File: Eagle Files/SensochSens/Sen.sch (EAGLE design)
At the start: 15 parts, among them U2 MIC5219, X1 ADC0-7

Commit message: 
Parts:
- removed C5: 1uF, SparkFun-Passives:CAP0402-CAP
- removed I2C_BUS: I2C_BUS, SparkFun-Connectors:M021X02_NO_SILK
- removed LED2: RED, SparkFun-LED:LED0603
- removed R6: 1k, SparkFun-Passives:RESISTOR0402-RES
- removed RN1: (no value), resistor-net:RN08
- removed X1: ADC0-7, con-molex:53047-10
- added C2: 10uF, SparkFun-Passives:CAP_POL1206
- added JP3: I2C_BUS, SparkFun-Connectors:M021X02_NO_SILK
- added LED1: RED, SparkFun-LED:LED0603
- added R1: 100k, SparkFun-Passives:RESISTOR0402-RES
- added RN2: (no value), resistor-net:RN08
- added X2: ADC0-7, con-molex:53047-10
- C4: value 10uF -> 1uF; device SparkFun-Passives:CAP_POL1206 -> SparkFun-Passives:CAP0402-CAP
- JP1: value LIPO_charger -> FTDI_BASICPTH; device jumper:JP4E -> SparkFun-Connectors:FTDI_BASICPTH
- JP2: value FTDI_BASICPTH -> LIPO_charger; device SparkFun-Connectors:FTDI_BASICPTH -> jumper:JP4E
- R2: value 100k -> 1k
- renumbered SMD1 to U1
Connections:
- removed net N$7: LED2.A, R6.1
- new net N$2: LED1.A, R2.1
- net 3.3V: now also C3.+, C4.1, JP1.4, R1.2, X2-1.S, X2-2.S; no longer C4.+, C5.1, JP2.4, R6.2, X1-1.S, X1-2.S
- net ADC0: now also RN2.2, X2-3.S; no longer RN1.2, X1-3.S
- net ADC1: now also RN2.3, X2-4.S; no longer RN1.3, X1-4.S
- net ADC2: now also RN2.4, X2-5.S; no longer RN1.4, X1-5.S
- net ADC3: now also RN2.5, X2-6.S; no longer RN1.5, X1-6.S
- net ADC4: now also RN2.6, X2-7.S; no longer RN1.6, X1-7.S
- net ADC5: now also RN2.7, X2-8.S; no longer RN1.7, X1-8.S
- net ADC6: now also RN2.8, X2-9.S; no longer RN1.8, X1-9.S
- net ADC7: now also RN2.9, X2-10.S; no longer RN1.9, X1-10.S
- net CTS2: now also JP1.5; no longer JP2.5
- net EN: now also JP2.4; no longer JP1.4
- net GND: now also C2.-, C4.2, JP1.6, JP2.3, LED1.C, RN2.1; no longer C4.-, C5.2, JP1.3, JP2.6, LED2.C, RN1.1
- net PS: now also JP2.1; no longer JP1.1
- net RESET: now also R1.1; no longer R2.1
- net RTS2: now also JP1.1; no longer JP2.1
- net RX2: now also JP1.3; no longer JP2.3
- net SCL: now also JP3.2; no longer I2C_BUS.2
- net SDA: now also JP3.1; no longer I2C_BUS.1
- net TX2: now also JP1.2; no longer JP2.2
- net VBATT: now also JP2.2; no longer JP1.2
- net VIN: now also C2.+; no longer C3.+
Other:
- note added: "ADC CKT"
- note added: "Connectors"
- note added: "Design by : Kartik Karuna (Kartik@kth.se)"
- note added: "Synapse Wireless SM700"
- note added: "Voltage Regulator"
- moved on the sheet: C1, C3, R2, S1, U2

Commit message: 
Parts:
- added LED2: GREEN, SparkFun-LED:LED0603
- added LED3: YELLOW, SparkFun-LED:LED0603
- added LED4: BLUE, SparkFun-LED:LED0603
- added R3, R4, R5: 330, SparkFun-Passives:RESISTOR0402-RES
- RN2: value (none) -> 22K
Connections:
- removed net N$10: U1.GPIO49_TD0
- removed net N$11: U1.GPIO48_TDI
- removed net N$12: U1.GPIO47_TCK
- new net LED2: LED2.A, U1.GPIO49_TD0
- new net LED3: LED3.A, U1.GPIO48_TDI
- new net LED4: LED4.A, U1.GPIO47_TCK
- new net N$1: LED3.C, R4.2
- new net N$4: LED2.C, R3.2
- new net N$6: LED4.C, R5.2
- net GND: now also R3.1, R4.1, R5.1
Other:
- note added: "LEDS"

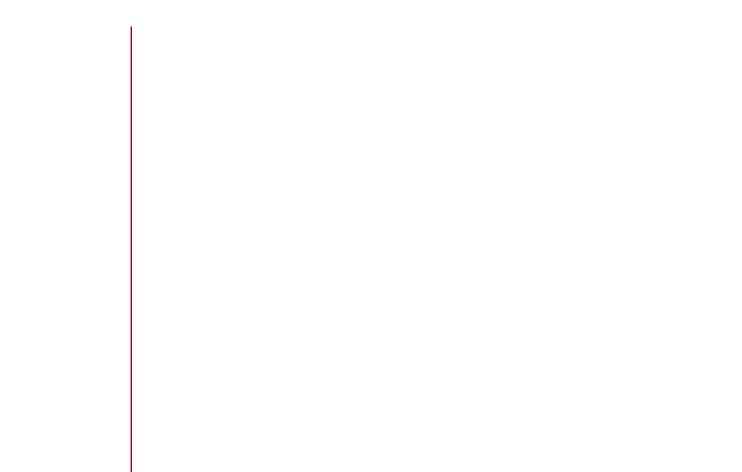
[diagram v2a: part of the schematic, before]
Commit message: 
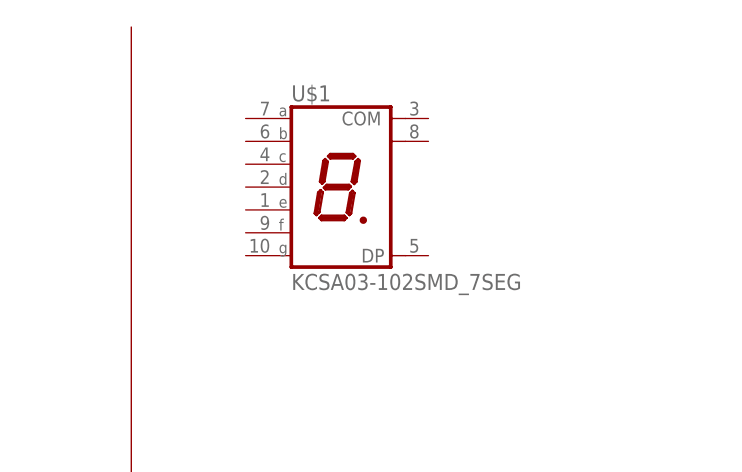
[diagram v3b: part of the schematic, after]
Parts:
- added U$1: KCSA03-102SMD_7SEG, cy-7-seg:KCSA03-102SMD_7SEG
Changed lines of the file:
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@@
 <part name="LED4" library="SparkFun-LED" deviceset="LED" device="0603" value="BLUE"/>
 <part name="R5" library="SparkFun-Passives" deviceset="RESISTOR" device="0402-RES" value="330"/>
+<part name="U$1" library="cy-7-seg" deviceset="KCSA03-102" device="SMD_7SEG"/>
 </parts>
 <sheets>
@@
 <instance part="LED4" gate="G$1" x="-48.26" y="147.32"/>
 <instance part="R5" gate="G$1" x="-48.26" y="134.62" rot="R90"/>
+<instance part="U$1" gate="G$1" x="203.2" y="200.66"/>
 </instances>
 <busses>

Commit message: 
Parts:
- added CH, DIV_ID: (no value), switch-dil:A1353HEX
- added R6, R7: 330, SparkFun-Passives:RESISTOR0402-RES
- added S2: RESET, cy_fsmsm:TYCO_FSMSFSMSM
- added S3: (no value), switch:A68-A31
- added S4: TOGGLE, cy_fsmsm:TYCO_FSMRACDA
- JP1: value FTDI_BASICPTH -> FTDI
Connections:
- new net 7SEG_A: U$1.A, U1.GPIO22_KBI_0_HST_WK
- new net 7SEG_B: U$1.B, U1.GPIO23_KBI_1
- new net 7SEG_C: U$1.C, U1.GPIO24_KBI_2
- new net 7SEG_D: U$1.D, U1.GPIO25_KBI_3
- new net 7SEG_DP: U$1.DP, U1.GPIO29_KBI_7
- new net 7SEG_E: U$1.E, U1.GPIO26_KBI_4
- new net 7SEG_F: U$1.F, U1.GPIO27_KBI_5
- new net 7SEG_G: U$1.G, U1.GPIO28_KBI_6
- new net CH_1: CH.1, U1.GPIO8_TMR0
- new net CH_2: CH.2, U1.GPIO9_TMR1
- new net CH_3: CH.4, U1.GPIO10_TMR2
- new net CH_4: CH.8, U1.GPIO11_TMR3
- new net DIV_1: DIV_ID.1, U1.GPIO2_SSI_FSYN
- new net DIV_2: DIV_ID.2, U1.GPIO3_SSI_BITCK
- new net DIV_3: DIV_ID.4, U1.GPIO4_SPI_SS
- new net DIV_4: DIV_ID.8, U1.GPIO5_SPI_MISO
- new net N$3: R6.2, U$1.COM@1
- new net N$5: R7.2, U$1.COM@2
- new net TOGL: S4.1, U1.GPIO46_TMS
- new net VCC1: S1.S, S3A.O
- net 3.3V: now also CH.C, DIV_ID.C, R6.1, R7.1, S4.2
- net EN: now also S3B.P
- net GND: now also S2.1, S3B.S
- net RESET: now also S2.2
- net VBATT: now also S3A.P, S3B.O; no longer S1.S
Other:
- note added: "7 SEGMENT"
- note added: "BUTTONS & SW"
- note added: "Rotary DIP Switch"
- moved on the sheet: S1

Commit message: 
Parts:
- removed X2: ADC0-7, con-molex:53047-10
- added JP4: M05X2SHD_LOCK, SparkFun-Connectors:M05X2SHD_LOCK
- C1: device SparkFun-Passives:CAP0402-CAP -> SparkFun-Passives:CAP0603-CAP
- C2, C3: device SparkFun-Passives:CAP_POL1206 -> SparkFun-Passives:CAP_POL3528
- CH, DIV_ID: value (none) -> HIX DIP
- JP2: value LIPO_charger -> LIPO
- R1, R2: device SparkFun-Passives:RESISTOR0402-RES -> SparkFun-Passives:RESISTOR0805-RES
- R3, R4, R5, R6, R7: device SparkFun-Passives:RESISTOR0402-RES -> SparkFun-Passives:RESISTOR0603-RES
- S1: value (none) -> Secondary sw
- S3: value (none) -> Primary sw
- renumbered U$1 to U3
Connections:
- net 3.3V: now also JP4.1, JP4.10; no longer X2-1.S, X2-2.S
- net ADC0: now also JP4.2; no longer X2-3.S
- net ADC1: now also JP4.3; no longer X2-4.S
- net ADC2: now also JP4.4; no longer X2-5.S
- net ADC3: now also JP4.5; no longer X2-6.S
- net ADC4: now also JP4.6; no longer X2-7.S
- net ADC5: now also JP4.7; no longer X2-8.S
- net ADC6: now also JP4.8; no longer X2-9.S
- net ADC7: now also JP4.9; no longer X2-10.S
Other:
- note added: "Design by: Kartik Karuna (Kartik@kth.se)"
- note removed: "Design by : Kartik Karuna (Kartik@kth.se)"
